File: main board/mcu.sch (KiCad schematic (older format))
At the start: 4 parts, among them U4 MAX32630IWG+T

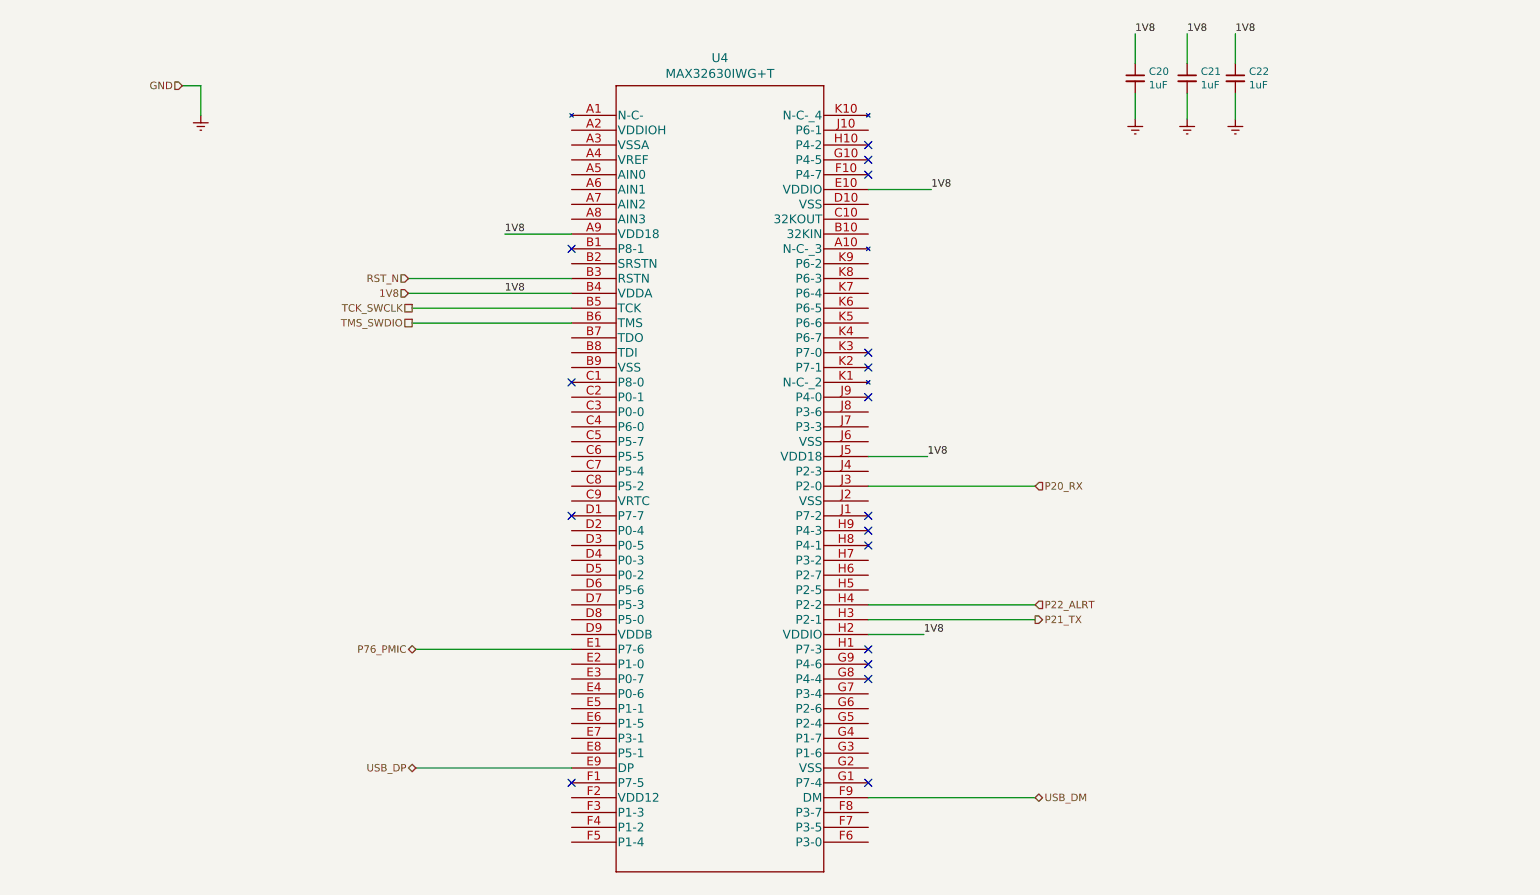
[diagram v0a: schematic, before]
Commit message: added crystal and motion sensor
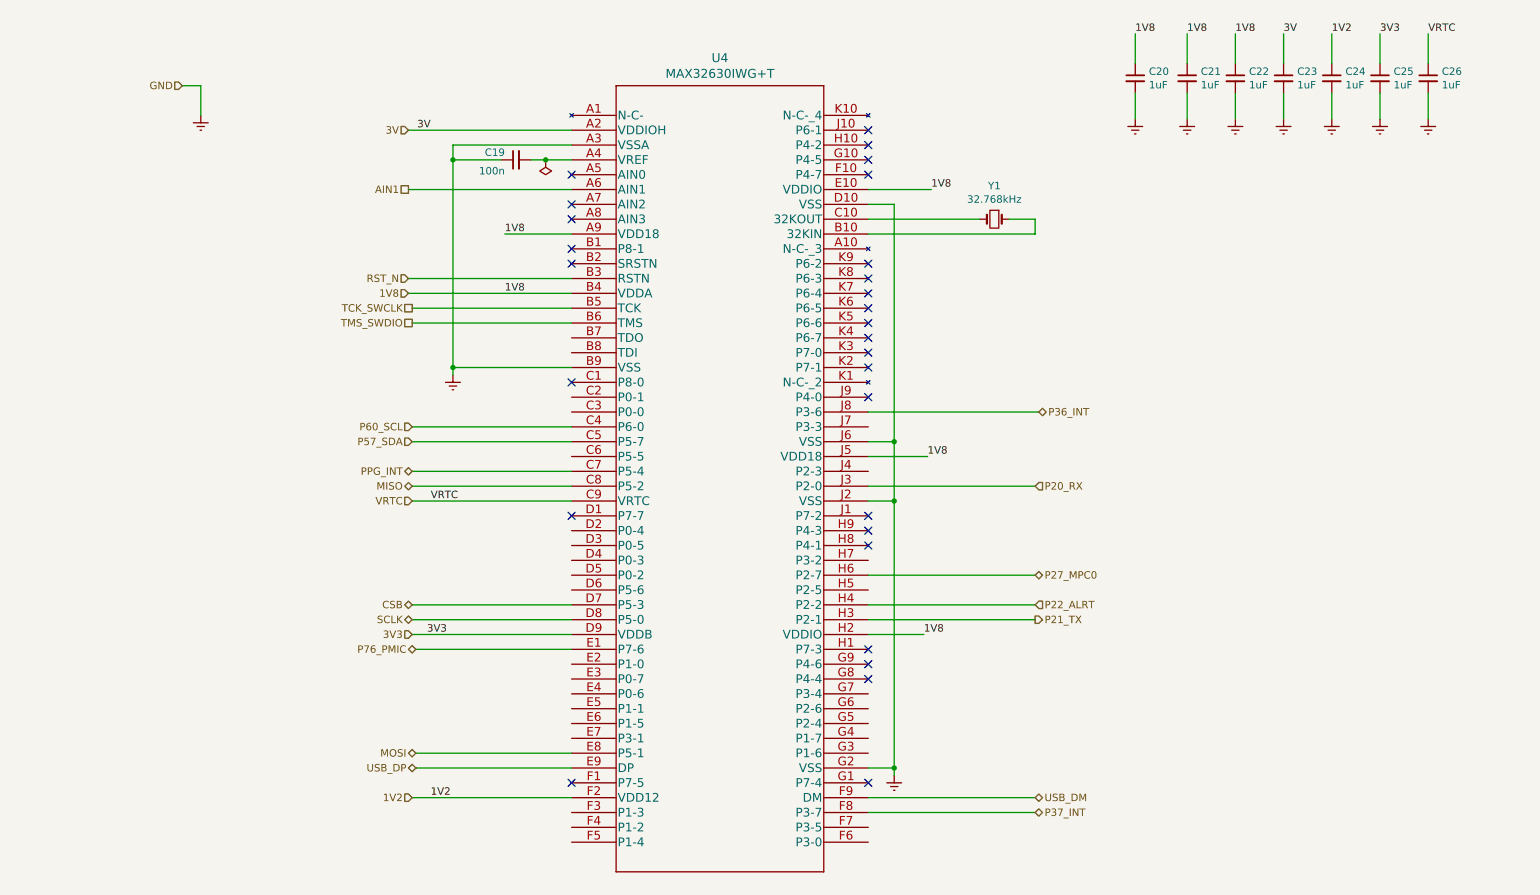
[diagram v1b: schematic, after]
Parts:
- added C19: 100n, symbol Device:C_Small
- added C23, C24, C25, C26: 1uF, symbol Device:C_Small
- added Y1: 32.768kHz, Horace:XTAL320X150X90, symbol Device:Crystal_Small
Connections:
- net GNDREF: now also U4.A3 (VSSA), U4.B9 (VSS), U4.D10 (VSS), U4.G2 (VSS), U4.J2 (VSS), U4.J6 (VSS), C19.1, C23.2, C24.2, C25.2, C26.2
- net 3V: now reaches U4.A2 (VDDIOH)
- net 3V: now also C23.1
- net at U4.A4 (VREF): now also C19.2
- net AIN1: now reaches U4.A6 (AIN1)
- net at U4.B10 (32KIN): now also Y1.1
- net at U4.C10 (32KOUT): now also Y1.2
- net P60_SCL: now reaches U4.C4 (P6-0)
- net P57_SDA: now reaches U4.C5 (P5-7)
- net PPG_INT: now reaches U4.C7 (P5-4)
- net MISO: now reaches U4.C8 (P5-2)
- net VRTC: now reaches U4.C9 (VRTC)
- net VRTC: now also C26.1
- net CSB: now reaches U4.D7 (P5-3)
- net SCLK: now reaches U4.D8 (P5-0)
- net 3V3: now reaches U4.D9 (VDDB)
- net 3V3: now also C25.1
- net MOSI: now reaches U4.E8 (P5-1)
- net 1V2: now reaches U4.F2 (VDD12)
- net 1V2: now also C24.1
- net P37_INT: now reaches U4.F8 (P3-7)
- net P27_MPC0: now reaches U4.H6 (P2-7)
- net P36_INT: now reaches U4.J8 (P3-6)
- no-connect marks 17 -> 28

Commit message: added VRTC power input
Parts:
- added SW2: SW_Push, symbol Switch:SW_Push
- renumbered C19 to C22, C20 to C23, C21 to C24, C22 to C25, C23 to C26, C24 to C27, C25 to C28, C26 to C29, U4 to U5
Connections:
- net GNDREF: now also SW2.2
- net at U5.J4 (P2-3): now also SW2.1
- no-connect marks 28 -> 32
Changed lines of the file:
@@
 $EndComp
 $Comp
-L Device:C_Small C20
+L Device:C_Small C23
 U 1 1 60323852
 P 8250 1175
-F 0 "C20" H 8342 1221 50  0000 L CNN
+F 0 "C23" H 8342 1221 50  0000 L CNN
 F 1 "1uF" H 8342 1130 50  0000 L CNN
 F 2 "" H 8250 1175 50  0001 C CNN
@@
 1V8
 $Comp
-L Device:C_Small C21
+L Device:C_Small C24
 U 1 1 60329B52
 P 8600 1175
-F 0 "C21" H 8692 1221 50  0000 L CNN
+F 0 "C24" H 8692 1221 50  0000 L CNN
 F 1 "1uF" H 8692 1130 50  0000 L CNN
 F 2 "" H 8600 1175 50  0001 C CNN
@@
 	4450 2225 4000 2225
 $Comp
-L Device:C_Small C22
+L Device:C_Small C25
 U 1 1 6032BB4C
 P 8925 1175
-F 0 "C22" H 9017 1221 50  0000 L CNN
+F 0 "C25" H 9017 1221 50  0000 L CNN
 F 1 "1uF" H 9017 1130 50  0000 L CNN
 F 2 "" H 8925 1175 50  0001 C CNN
@@
 3V
 $Comp
-L Device:C_Small C23
+L Device:C_Small C26
 U 1 1 6034AE3B
 P 9250 1175
-F 0 "C23" H 9342 1221 50  0000 L CNN
+F 0 "C26" H 9342 1221 50  0000 L CNN
 F 1 "1uF" H 9342 1130 50  0000 L CNN
 F 2 "" H 9250 1175 50  0001 C CNN
@@
 1V2
 $Comp
-L Device:C_Small C24
+L Device:C_Small C27
 U 1 1 603435A7
 P 9575 1175
-F 0 "C24" H 9667 1221 50  0000 L CNN
+F 0 "C27" H 9667 1221 50  0000 L CNN
 F 1 "1uF" H 9667 1130 50  0000 L CNN
 F 2 "" H 9575 1175 50  0001 C CNN
@@
 3V3
 $Comp
-L Device:C_Small C25
+L Device:C_Small C28
 U 1 1 60347034
 P 9900 1175
-F 0 "C25" H 9992 1221 50  0000 L CNN
+F 0 "C28" H 9992 1221 50  0000 L CNN
 F 1 "1uF" H 9992 1130 50  0000 L CNN
 F 2 "" H 9900 1175 50  0001 C CNN
@@
 VRTC
 $Comp
-L Device:C_Small C26
+L Device:C_Small C29
 U 1 1 6034C536
 P 10225 1175
-F 0 "C26" H 10317 1221 50  0000 L CNN
+F 0 "C29" H 10317 1221 50  0000 L CNN
 F 1 "1uF" H 10317 1130 50  0000 L CNN
 F 2 "" H 10225 1175 50  0001 C CNN
@@
 Connection ~ 3650 3125
 $Comp
-L Device:C_Small C19
+L Device:C_Small C22
 U 1 1 6035F901
 P 4075 1725
-F 0 "C19" V 4125 1800 50  0000 L CNN
+F 0 "C22" V 4125 1800 50  0000 L CNN
 F 1 "100n" V 4000 1800 50  0000 L CNN
 F 2 "" H 4075 1725 50  0001 C CNN
@@
 P27_MPC0
 $Comp
-L Horace:MAX32630IWG+T U4
+L Horace:MAX32630IWG+T U5
 U 1 1 6001B2A5
 P 4450 1425
-F 0 "U4" H 5450 1812 60  0000 C CNN
+F 0 "U5" H 5450 1812 60  0000 C CNN
 F 1 "MAX32630IWG+T" H 5450 1706 60  0000 C CNN
 F 2 "Horace:MAX32630IWG&plus_T" H 5450 1665 60  0001 C CNN
@@
 Wire Wire Line
 	6450 3425 7600 3425
+$Comp
+L Switch:SW_Push SW2
+U 1 1 607226F2
+P 8125 3825
+F 0 "SW2" H 8125 4110 50  0000 C CNN
+F 1 "SW_Push" H 8125 4019 50  0000 C CNN
+F 2 "" H 8125 4025 50  0001 C CNN
+F 3 "~" H 8125 4025 50  0001 C CNN
+	1    8125 3825
+	1    0    0    -1
+$EndComp
+Wire Wire Line
+	6450 3825 7925 3825
+$Comp
+L power:GNDREF #PWR0169
+U 1 1 60724935
+P 8450 3975
+F 0 "#PWR0169" H 8450 3725 50  0001 C CNN
+F 1 "GNDREF" H 8455 3802 50  0001 C CNN
+F 2 "" H 8450 3975 50  0001 C CNN
+F 3 "" H 8450 3975 50  0001 C CNN
+	1    8450 3975
+	1    0    0    -1
+$EndComp
+Wire Wire Line
+	8450 3825 8450 3975
+Wire Wire Line
+	8325 3825 8450 3825
+NoConn ~ 6450 3525
+NoConn ~ 6450 4425
+NoConn ~ 6450 6325
+NoConn ~ 4450 5625
 $EndSCHEMATC

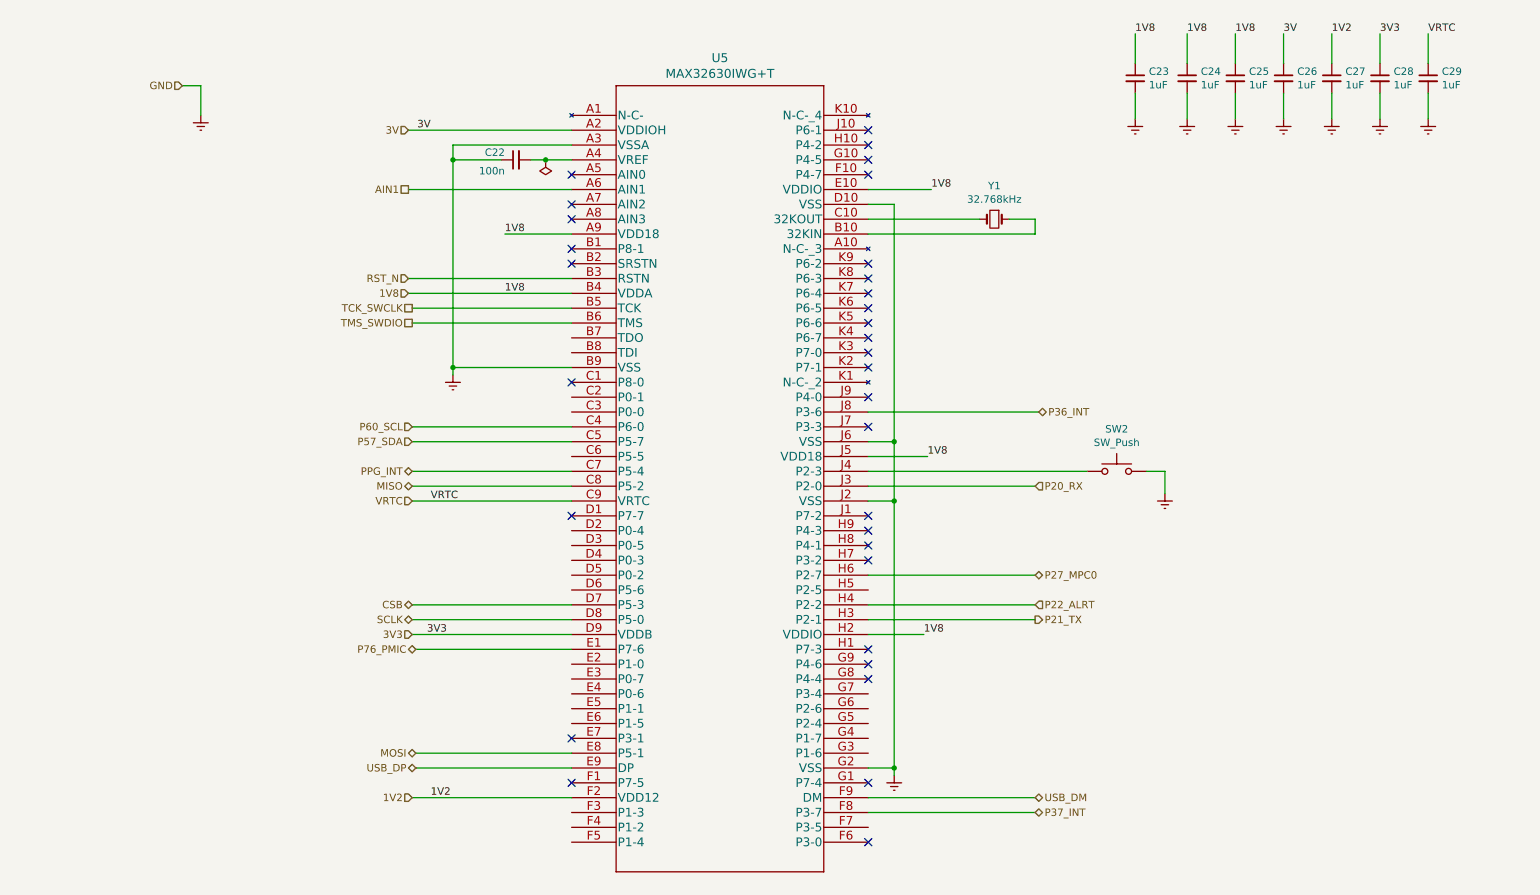
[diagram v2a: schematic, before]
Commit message: added flash and LED
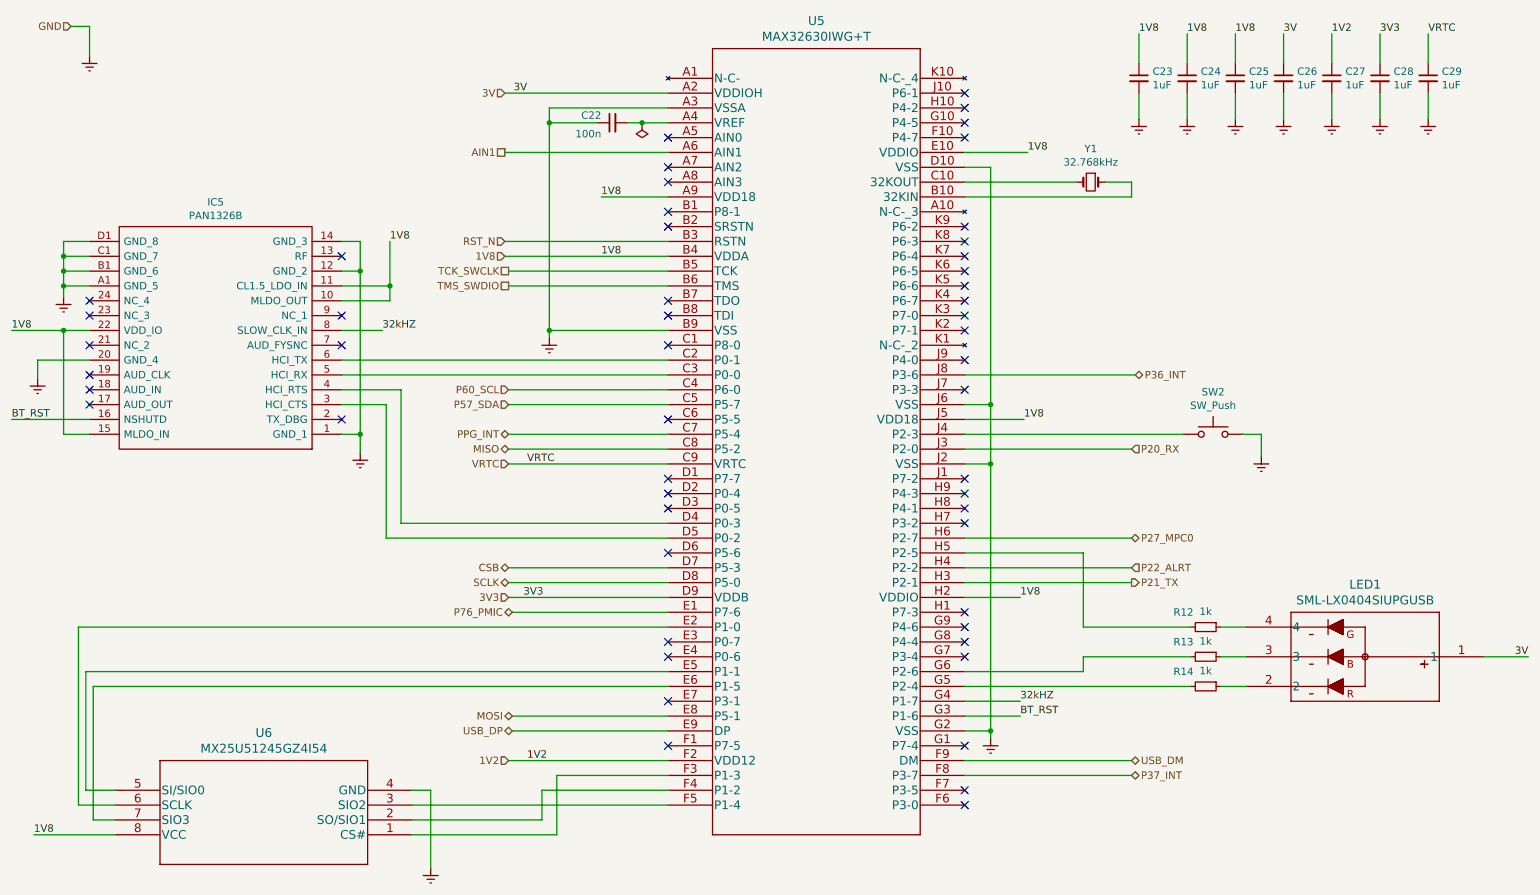
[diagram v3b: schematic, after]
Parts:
- added IC5: PAN1326B, Horace:PAN1326B, symbol Horace:PAN1326B
- added LED1: SML-LX0404SIUPGUSB, Horace:SML-LX0404SIUPGUSB, symbol Horace:SML-LX0404SIUPGUSB
- added R12, R13, R14: 1k, symbol Device:R_Small
- added U6: MX25U51245GZ4I54, Horace:MX25U51245GZ4I54, symbol Horace:MX25U51245GZ4I54
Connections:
- net 1V8: now also IC5.10 (MLDO_OUT), IC5.11 (CL1.5_LDO_IN), IC5.15 (MLDO_IN), IC5.22 (VDD_IO), U6.8 (VCC)
- net 3V: now also LED1.1
- net GNDREF: now also IC5.1 (GND_1), IC5.12 (GND_2), IC5.14 (GND_3), IC5.20 (GND_4), IC5.A1 (GND_5), IC5.B1 (GND_6), IC5.C1 (GND_7), IC5.D1 (GND_8), U6.4 (GND)
- net at U5.C2 (P0-1): now also IC5.6 (HCI_TX)
- net at U5.C3 (P0-0): now also IC5.5 (HCI_RX)
- net at U5.D4 (P0-3): now also IC5.4 (HCI_RTS)
- net at U5.D5 (P0-2): now also IC5.3 (HCI_CTS)
- net at U5.E2 (P1-0): now also U6.6 (SCLK)
- net at U5.E5 (P1-1): now also U6.5 (SI/SIO0)
- net at U5.E6 (P1-5): now also U6.7 (SIO3)
- net at U5.F3 (P1-3): now also U6.1 (CS#)
- net at U5.F4 (P1-2): now also U6.2 (SO/SIO1)
- net at U5.F5 (P1-4): now also U6.3 (SIO2)
- net BT_RST: now reaches U5.G3 (P1-6)
- net BT_RST: now also IC5.16 (NSHUTD)
- net 32kHZ: now reaches U5.G4 (P1-7)
- net 32kHZ: now also IC5.8 (SLOW_CLK_IN)
- net at U5.G5 (P2-4): now also R14.2
- net at U5.G6 (P2-6): now also R13.2
- net at U5.H5 (P2-5): now also R12.2
- new net: LED1.2, R14.1
- new net: LED1.3, R13.1
- new net: LED1.4, R12.1
- no-connect marks 32 -> 52
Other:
- moved on the sheet: C22, C23, SW2, U5, Y1

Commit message: added 100n capacitor
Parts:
- C22: footprint (none) -> Capacitor_SMD:C_0402_1005Metric; Digikey Part Number (none) -> 311-3340-2-ND; Mouser Price/Stock (none) -> https://www.mouser.ee/ProductDetail/Yageo/CC0402KRX5R5BB104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; Price (none) -> 0.09
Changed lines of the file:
@@
 F 0 "C22" V 4775 1550 50  0000 L CNN
 F 1 "100n" V 4650 1550 50  0000 L CNN
-F 2 "" H 4725 1475 50  0001 C CNN
-F 3 "~" H 4725 1475 50  0001 C CNN
+F 2 "Capacitor_SMD:C_0402_1005Metric" H 4725 1475 50  0001 C CNN
+F 3 "https://www.mouser.ee/datasheet/2/447/UPY_GPHC_X5R_4V_to_50V_25-1131599.pdf" H 4725 1475 50  0001 C CNN
+F 4 "https://www.mouser.ee/ProductDetail/Yageo/CC0402KRX5R5BB104/?qs=T%2F3nPWKqOSbG4z8ii3LyCg%3D%3D" V 4725 1475 50  0001 C CNN "Mouser Price/Stock"
+F 5 "311-3340-2-ND" V 4725 1475 50  0001 C CNN "Digikey Part Number"
+F 6 "0.09" V 4725 1475 50  0001 C CNN "Price"
 	1    4725 1475
 	0    -1   -1   0

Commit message: mcu parts
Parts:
- removed SW2: SW_Push, symbol Switch:SW_Push
- added C30: 100n, Capacitor_SMD:C_0402_1005Metric, symbol Device:C_Small
- added S2: 434153017835, Horace:434153017835, symbol Horace:434153017835
- C23, C24, C25, C26, C27, C28, C29: footprint (none) -> Capacitor_SMD:C_0402_1005Metric; Digikey Part Number (none) -> 311-1438-2-ND; Mouser Price/Stock (none) -> https://www.mouser.ee/ProductDetail/Yageo/CC0402KRX5R5BB105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; Price (none) -> 0.09
- IC5: Digikey Part Number (none) -> P16860TR-ND; Mouser Price/Stock (none) -> https://www.mouser.ee/ProductDetail/Panasonic/ENW-89823A3KF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; Price (none) -> 12.19
- LED1: Digikey Part Number (none) -> 67-2125-1-ND; Mouser Price/Stock (none) -> https://www.mouser.ee/ProductDetail/Lumex/SML-LX0404SIUPGUS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; Price (none) -> 0.86
- R12, R13, R14: footprint (none) -> Resistor_SMD:R_0402_1005Metric; Digikey Part Number (none) -> 541-4279-2-ND; Mouser Price/Stock (none) -> https://www.mouser.ee/ProductDetail/Vishay-Dale/CRCW01001K0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; Price (none) -> 0.14
- U5: Digikey Part Number (none) -> MAX32630IWG+TCT-ND; Mouser Price/Stock (none) -> https://www.mouser.ee/ProductDetail/Maxim-Integrated/MAX326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; Price (none) -> 10.43
- U6: Digikey Part Number (none) -> 1092-1252-ND; Price (none) -> 10.03
- Y1: Digikey Part Number (none) -> 535-11898-1-ND; Mouser Price/Stock (none) -> https://www.mouser.ee/ProductDetail/ABRACON/ABS07-32768KHZ-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; Price (none) -> 0.63
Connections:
- net 1V8: now also C30.2
- net GNDREF: now also C30.1, S2.2, S2.4
- net at U5.J4 (P2-3): now also S2.1, S2.3
